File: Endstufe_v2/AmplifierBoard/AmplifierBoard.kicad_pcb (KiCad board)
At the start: 2 copper layers, 110 x 80 mm, 99 parts, among them J1 Conn_01x01_Pin, J11 B6B-XH-2(LF)(SN), J12 B6B-XH-2(LF)(SN), J13 Conn_01x02_Pin, J14 Conn_01x02_Pin, J15 Conn_01x02_Pin, J2 Conn_01x01_Pin, J3 banana connector, J4 banana connector, J5 banana connector, J6 banana connector, J7 banana connector, J8 banana connector, J9 ST-0322D00-071-1A2H, U1 TPA3126D2DADR, U2 TPA3126D2DADR, U3 NVTFWS014P04M8LTAG, U4 1SMA5927A

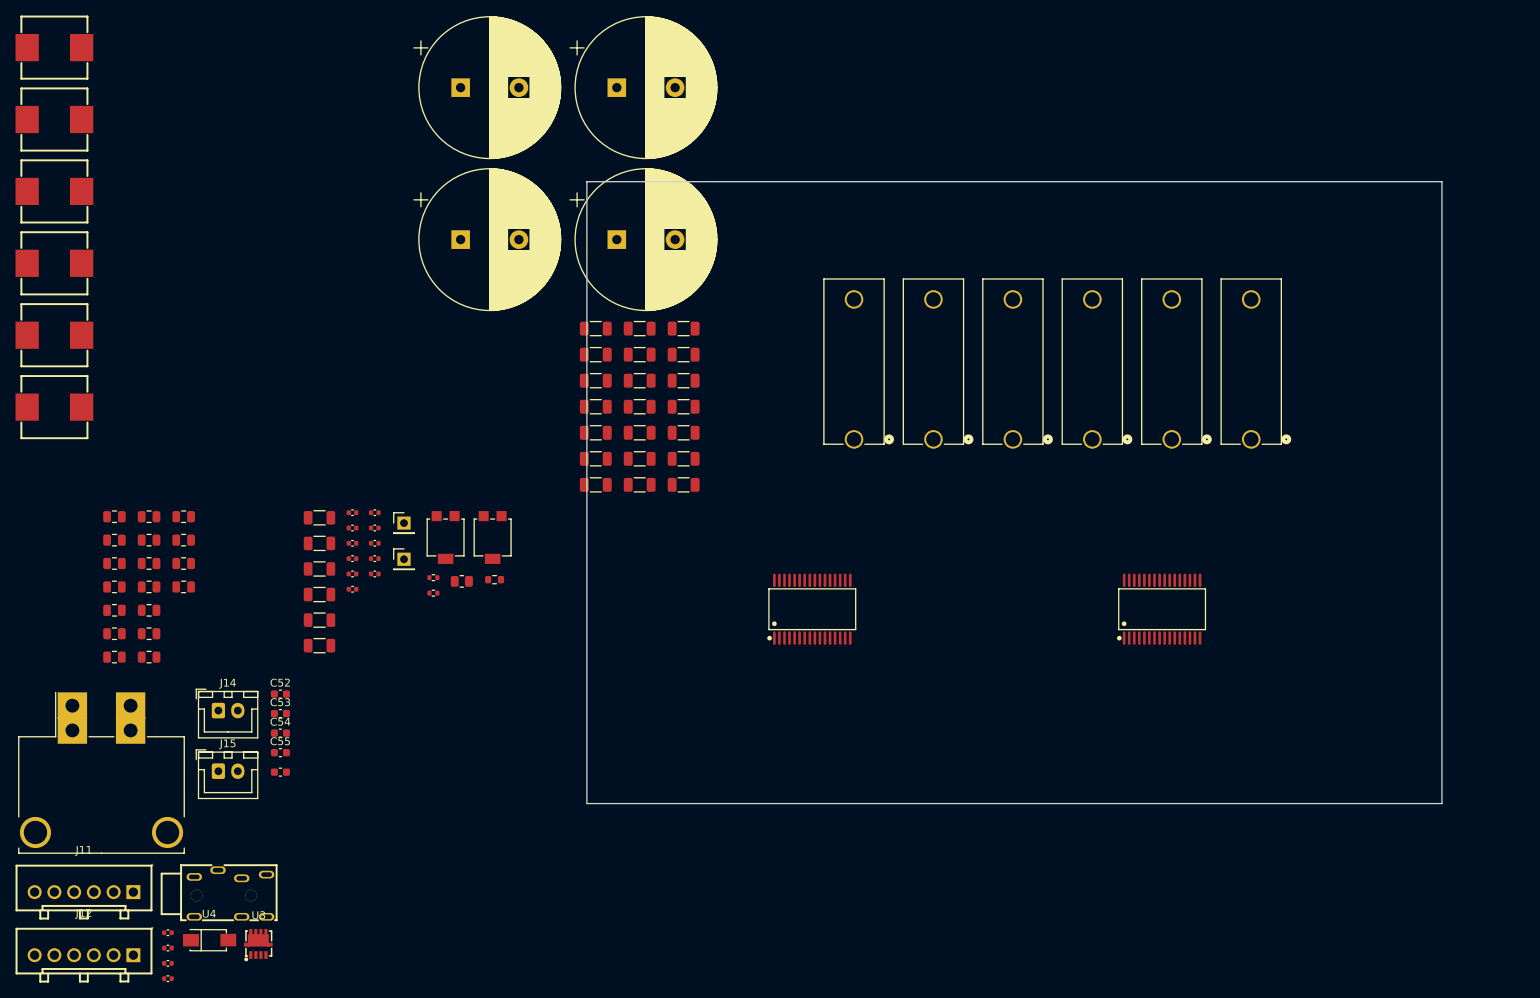
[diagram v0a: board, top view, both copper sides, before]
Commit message: Layout amplifier board
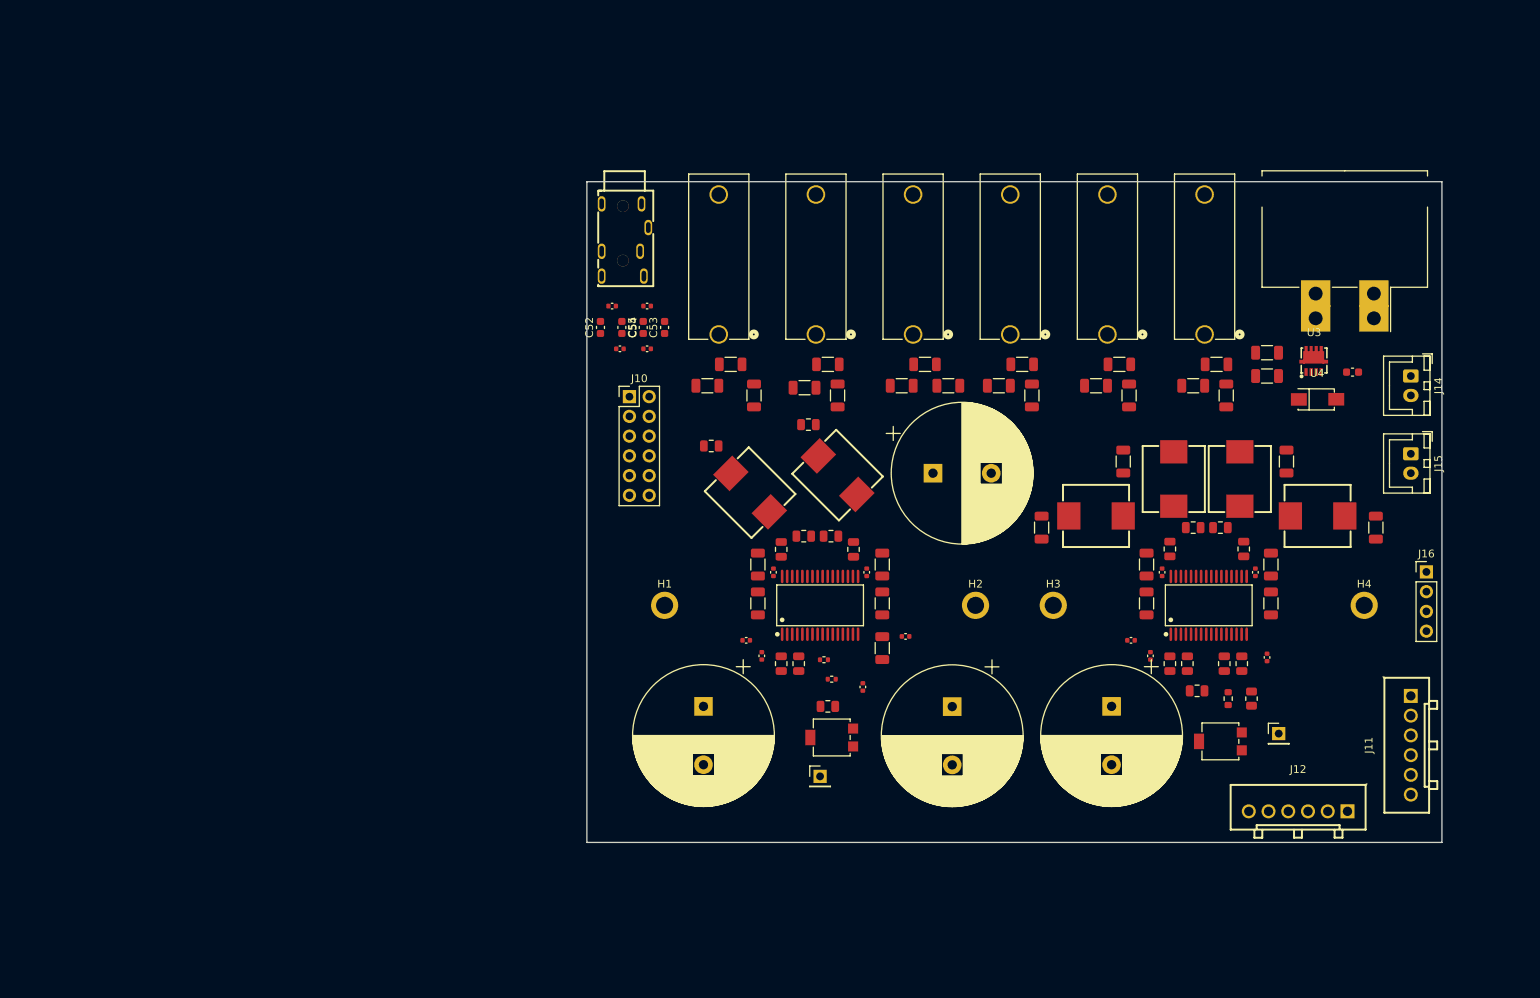
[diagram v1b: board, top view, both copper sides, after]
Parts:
- added C18: 10uF, Endstufe:C_1206_3216Metric, F.Cu at (228.0, 104.2)
- added C19: 10uF, Endstufe:C_1206_3216Metric, F.Cu at (212.0, 104.2)
- added C20: 10uF, Endstufe:C_1206_3216Metric, F.Cu at (178.0, 104.2)
- added C21: 10uF, Endstufe:C_1206_3216Metric, F.Cu at (162.0, 104.2)
- added C56: 10uF, Endstufe:C_1206_3216Metric, F.Cu at (227.5, 72.0)
- added C57: 10uF, Endstufe:C_1206_3216Metric, F.Cu at (227.5, 75.0)
- added H1: MountingHole_Pad, MountingHole:MountingHole_2.2mm_M2_ISO7380_Pad, F.Cu at (150.0, 104.5)
- added H2: MountingHole_Pad, MountingHole:MountingHole_2.2mm_M2_ISO7380_Pad, F.Cu at (190.0, 104.5)
- added H3: MountingHole_Pad, MountingHole:MountingHole_2.2mm_M2_ISO7380_Pad, F.Cu at (200.0, 104.5)
- added H4: MountingHole_Pad, MountingHole:MountingHole_2.2mm_M2_ISO7380_Pad, F.Cu at (240.0, 104.5)
- added J10: Conn_02x06_Top_Bottom, Connector_PinHeader_2.54mm:PinHeader_2x06_P2.54mm_Vertical, F.Cu at (145.5, 77.7)
- added J16: Conn_01x04, Connector_PinHeader_2.54mm:PinHeader_1x04_P2.54mm_Vertical, F.Cu at (248.0, 100.2)
- moved J13 176.6 mm to (241.2, 64.4), turned to 180 degrees
- moved J11 171.7 mm to (246.0, 122.5), turned to 90 degrees
- moved L4 165.7 mm to (234.0, 93.0)
- moved J14 159.3 mm to (246.0, 75.0), turned to -90 degrees
- moved J15 158.7 mm to (246.0, 85.0), turned to -90 degrees
- moved U4 158.6 mm to (234.0, 78.0)
- moved J12 157.3 mm to (231.5, 131.0)
- moved L3 156.9 mm to (224.0, 88.2), turned to 90 degrees
- moved U3 155.1 mm to (233.5, 73.0)
- moved L2 151.2 mm to (215.5, 88.2), turned to 90 degrees
- moved R22 147.2 mm to (238.5, 74.5)
- moved L1 146.9 mm to (205.5, 93.0), turned to 180 degrees
- moved C1 146.3 mm to (224.2, 112.0), turned to 90 degrees
- moved C2 143.7 mm to (222.0, 112.0), turned to 90 degrees
- moved C28 140.9 mm to (224.5, 97.2), turned to 90 degrees
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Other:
- board size 110 x 80 mm -> 110 x 85 mm
- board text added: "Blocked by heatsink"

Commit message: Continue layouting
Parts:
- moved J12 1.50 mm to (233.0, 131.0)
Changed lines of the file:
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@@
 	)
 	(footprint "Endstufe:CONN-TH_B6B-XH-2-LF-SN"
+		(locked yes)
 		(layer "F.Cu")
-		(at 231.5 131)
+		(at 233 131)
 		(descr "CONN-TH_B6B-XH-2-LF-SN footprint")
 		(tags "CONN-TH_B6B-XH-2-LF-SN footprint C157986")

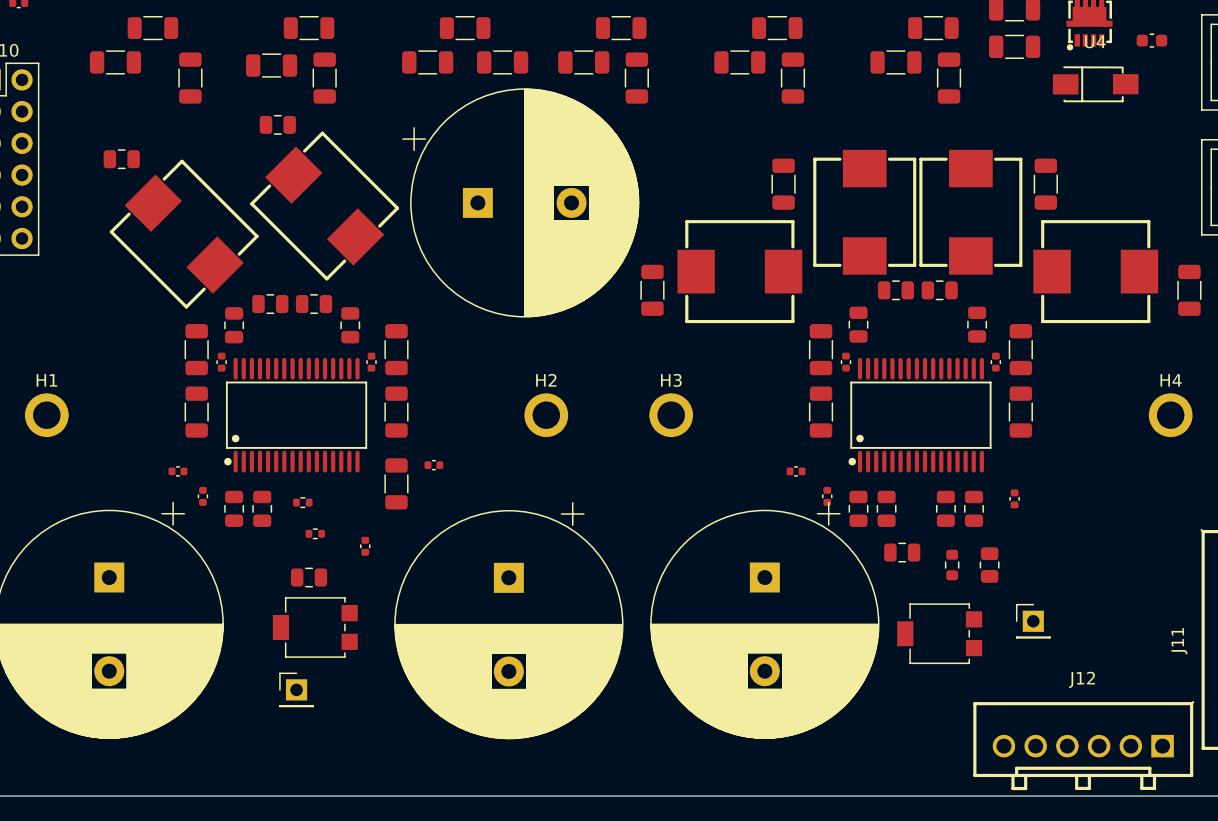
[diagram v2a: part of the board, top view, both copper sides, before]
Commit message: Make mounting holes and continue layouting
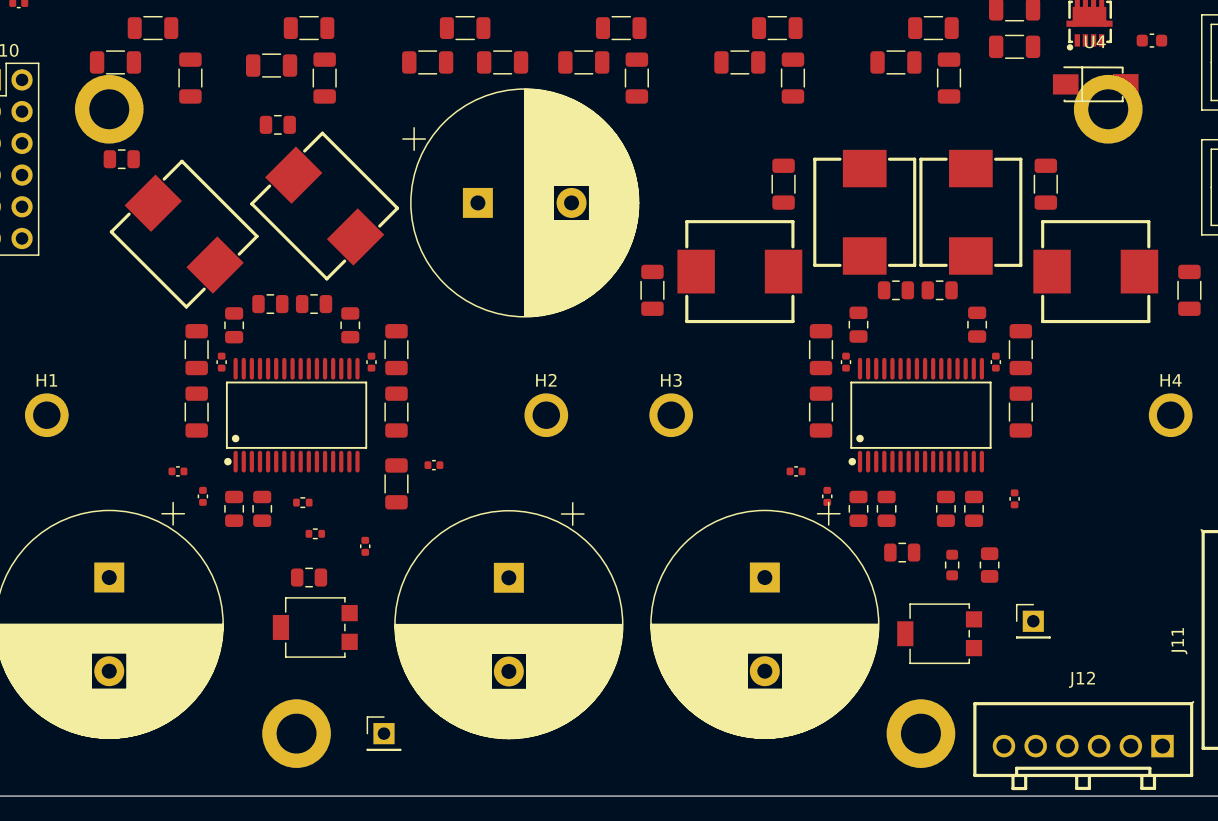
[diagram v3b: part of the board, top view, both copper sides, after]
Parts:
- added H5: MountingHole_Pad, Endstufe:MountingHole_3.2mm_M3_ISO14580_Pad, F.Cu at (155.0, 80.0)
- added H6: MountingHole_Pad, Endstufe:MountingHole_3.2mm_M3_ISO14580_Pad, F.Cu at (235.0, 80.0)
- added H7: MountingHole_Pad, Endstufe:MountingHole_3.2mm_M3_ISO14580_Pad, F.Cu at (220.0, 130.0)
- added H8: MountingHole_Pad, Endstufe:MountingHole_3.2mm_M3_ISO14580_Pad, F.Cu at (170.0, 130.0)
- moved J2 7.83 mm to (177.0, 130.0)

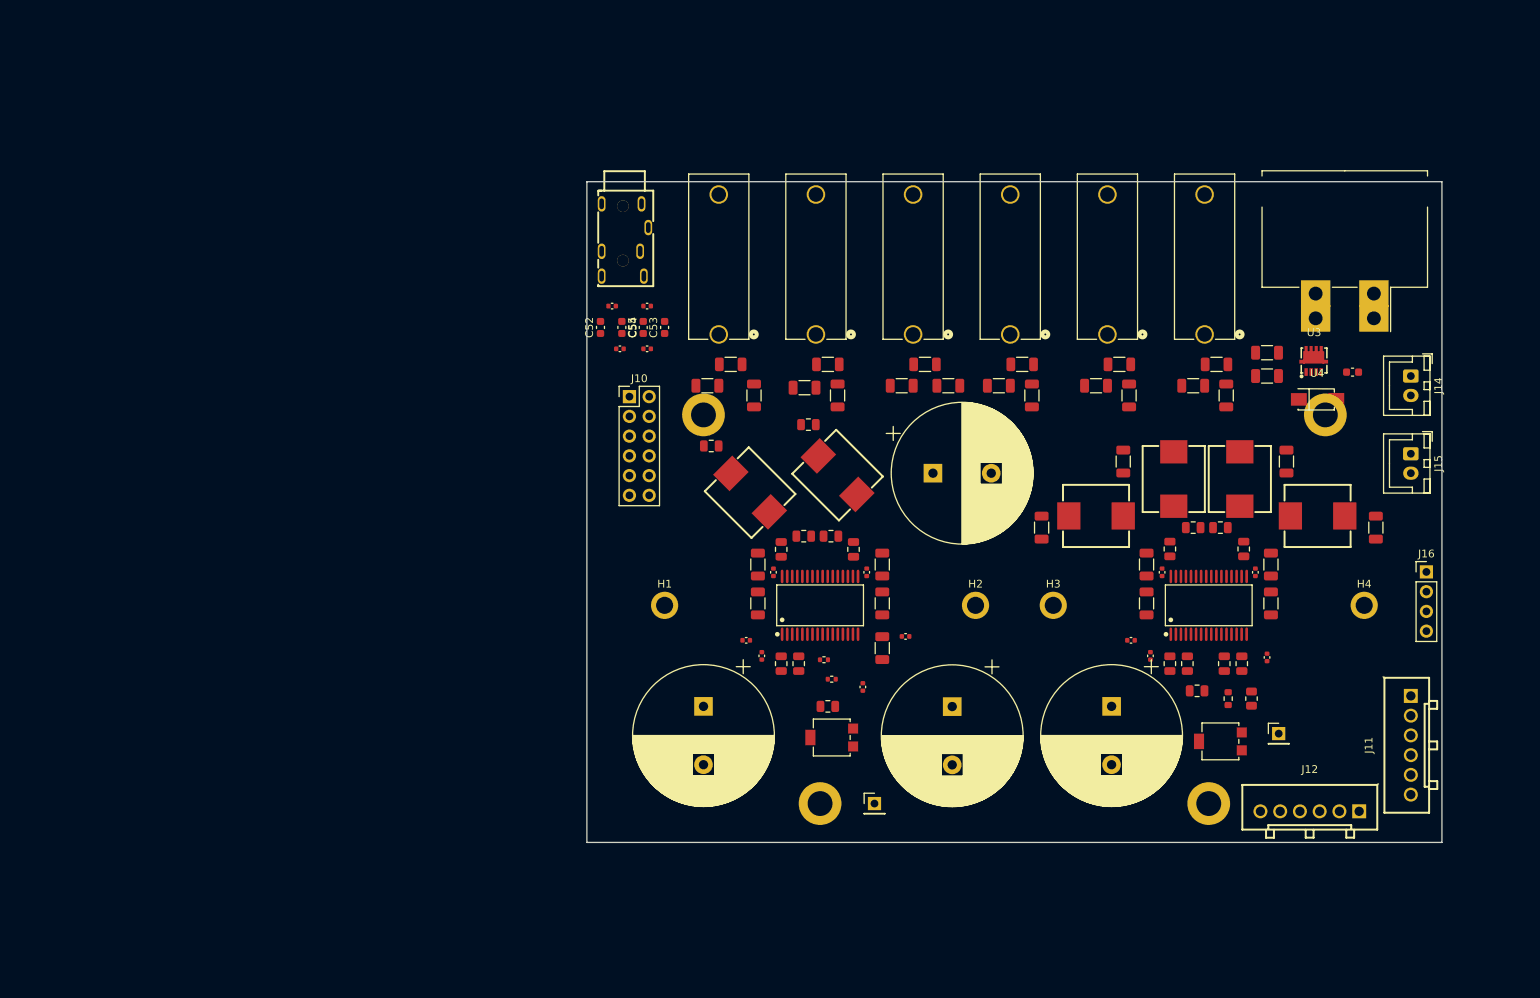
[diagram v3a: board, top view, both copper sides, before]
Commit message: Enlargen Amplifier Board to make space for mounting holes
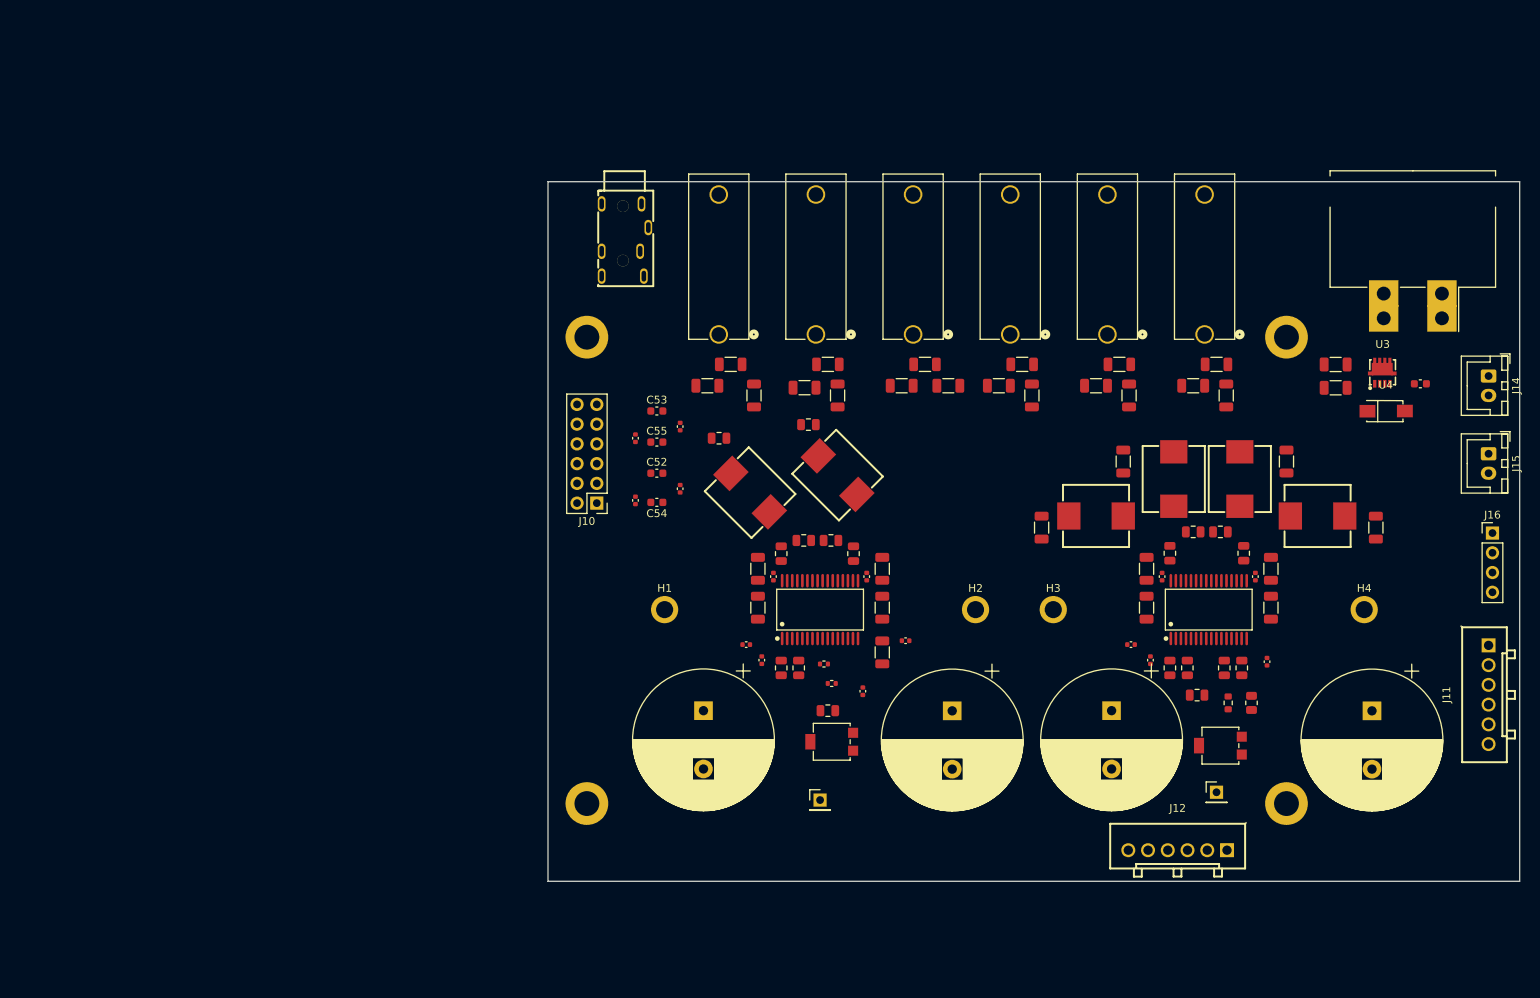
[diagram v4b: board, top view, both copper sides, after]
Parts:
- moved C23 64.2 mm to (241.0, 118.1), turned to -90 degrees
- moved H8 30.0 mm to (140.0, 130.0)
- moved R18 25.1 mm to (152.0, 89.5), turned to 90 degrees
- moved C54 22.9 mm to (149.0, 91.2), turned to 180 degrees
- moved C52 20.1 mm to (149.0, 87.5), turned to 0 degrees
- moved R21 19.6 mm to (146.2, 91.0), turned to 90 degrees
- moved H5 18.0 mm to (140.0, 70.0)
- moved J12 17.7 mm to (216.0, 136.0)
- moved R19 16.1 mm to (152.0, 81.5), turned to 90 degrees
- moved C55 14.9 mm to (149.0, 83.5), turned to 0 degrees
- moved J10 14.3 mm to (141.3, 91.3), turned to 180 degrees
- moved J11 11.9 mm to (256.0, 116.0)
- moved R20 11.6 mm to (146.2, 83.0), turned to 90 degrees
- moved H6 11.2 mm to (230.0, 70.0)
- moved J1 11.0 mm to (221.0, 128.6)
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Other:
- board size 110 x 85 mm -> 125 x 90 mm

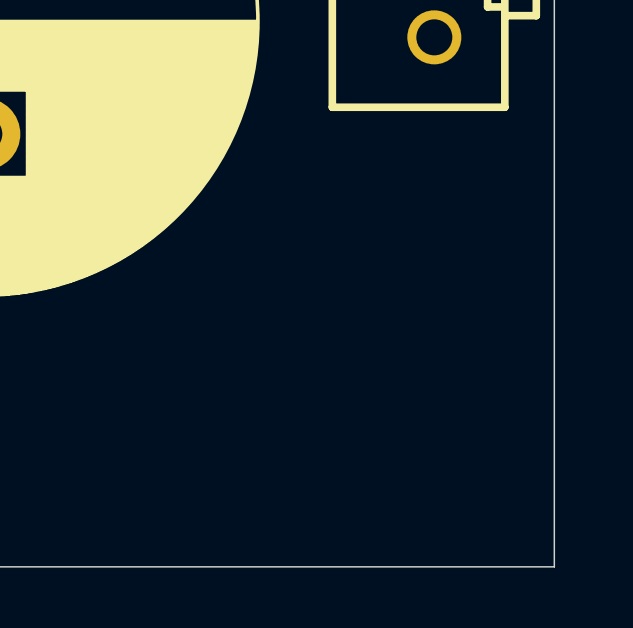
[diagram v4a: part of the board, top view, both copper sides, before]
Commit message: Add additional power connector to amplifier board
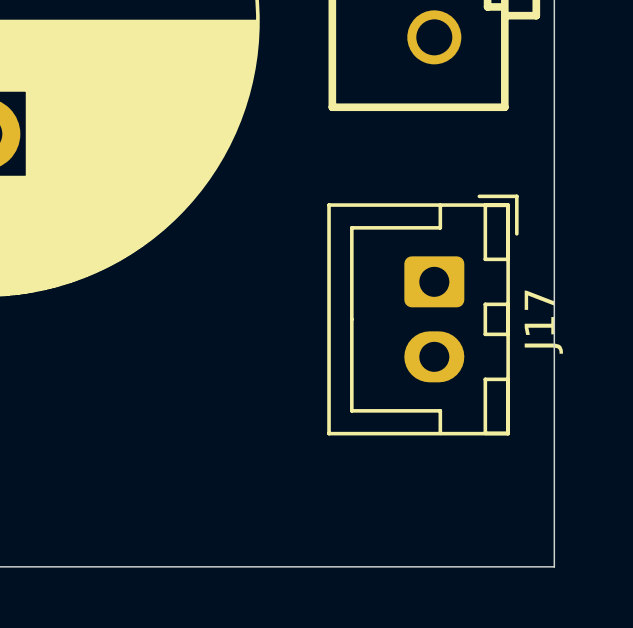
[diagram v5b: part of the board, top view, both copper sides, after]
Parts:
- added J17: Conn_01x02_Pin, Connector_JST:JST_XH_B2B-XH-A_1x02_P2.50mm_Vertical, F.Cu at (256.0, 130.5)
